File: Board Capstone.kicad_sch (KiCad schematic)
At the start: 12 parts, among them J101 Power, J102 Conn_JetsonNano, J103 Status_LED, J104 Warning_LED, SW101 SW_Pairing, U101 SN74LV1T125DBV, U102 SN74LV1T125DBV

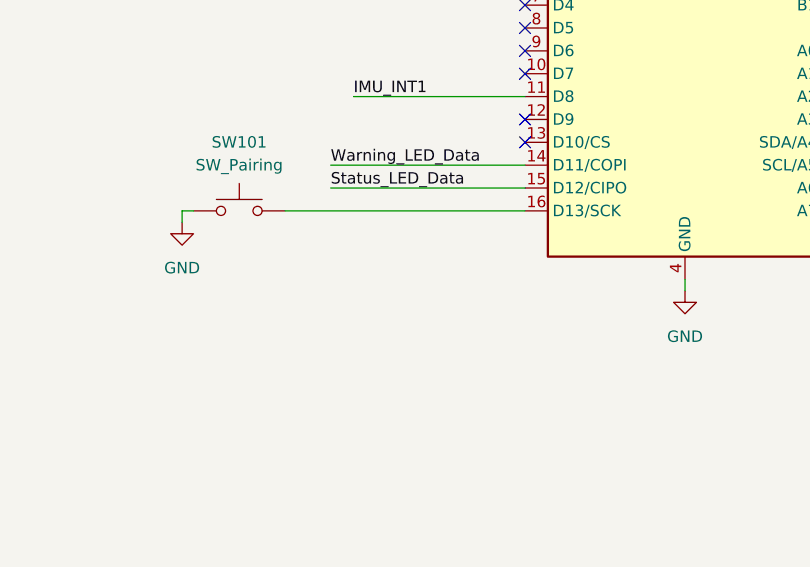
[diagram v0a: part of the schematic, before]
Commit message: rev 1.1.1 Added decoupling cap to push button
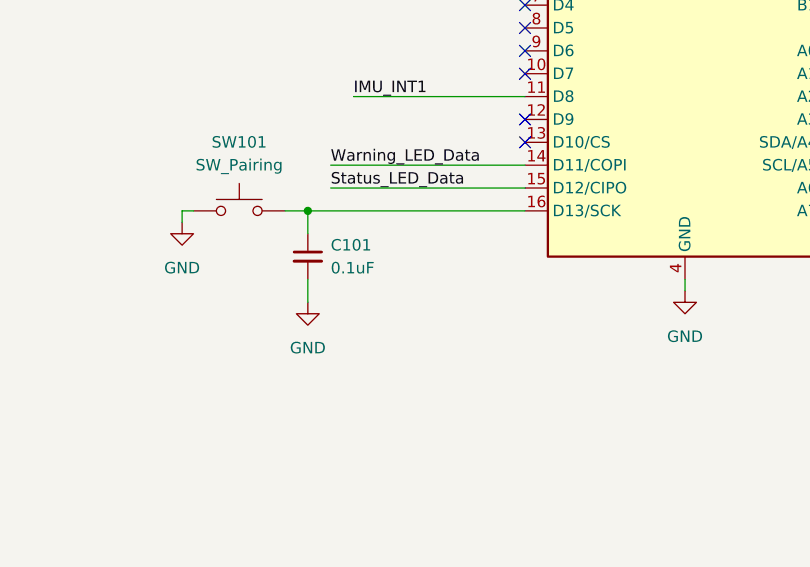
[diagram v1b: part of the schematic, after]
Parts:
- added C101: 0.1uF, Capacitor_SMD:C_1206_3216Metric_Pad1.33x1.80mm_HandSolder, symbol Device:C_Small
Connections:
- net GND: now also C101.2
- net at A101.16 (D13/SCK), SW101.2: now also C101.1
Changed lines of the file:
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@@
 		(title "Cyclops (Team 30)")
 		(date "2025-11-28")
-		(rev "1")
+		(rev "1.1.1")
 		(company "Concordia University, Department of Electrical and Computer Engineering")
 	)
@@
 	)
 	(junction
+		(at 111.76 83.82)
+		(diameter 0)
+		(color 0 0 0 0)
+	)
+	(junction
 		(at 208.28 76.2)
 		(diameter 0)
@@
 	(wire
 		(pts
+			(xy 111.76 83.82) (xy 135.89 83.82)
+		)
+		(stroke
+			(width 0)
+			(type default)
+		)
+	)
+	(wire
+		(pts
 			(xy 229.87 149.86) (xy 227.33 149.86)
 		)
@@
 	(wire
 		(pts
+			(xy 111.76 86.36) (xy 111.76 83.82)
+		)
+		(stroke
+			(width 0)
+			(type default)
+		)
+	)
+	(wire
+		(pts
 			(xy 24.13 41.91) (xy 24.13 43.18)
 		)
@@
 	(wire
 		(pts
-			(xy 109.22 83.82) (xy 135.89 83.82)
+			(xy 109.22 83.82) (xy 111.76 83.82)
 		)
 		(stroke
@@
 		(pts
 			(xy 24.13 45.72) (xy 24.13 46.99)
+		)
+		(stroke
+			(width 0)
+			(type default)
+		)
+	)
+	(wire
+		(pts
+			(xy 111.76 93.98) (xy 111.76 91.44)
 		)
 		(stroke
@@
 	(symbol
 		(lib_id "power:GND")
+		(at 111.76 93.98 0)
+		(unit 1)
+		(exclude_from_sim no)
+		(in_bom yes)
+		(on_board yes)
+		(dnp no)
+		(fields_autoplaced yes)
+		(property "Reference" "#PWR0122"
+			(at 111.76 100.33 0)
+			(effects
+				(font
+					(size 1.27 1.27)
+				)
+				(hide yes)
+			)
+		)
+		(property "Value" "GND"
+			(at 111.76 99.06 0)
+			(effects
+				(font
+					(size 1.27 1.27)
+				)
+			)
+		)
+		(property "Footprint" ""
+			(at 111.76 93.98 0)
+			(effects
+				(font
+					(size 1.27 1.27)
+				)
+				(hide yes)
+			)
+		)
+		(property "Datasheet" ""
+			(at 111.76 93.98 0)
+			(effects
+				(font
+					(size 1.27 1.27)
+				)
+				(hide yes)
+			)
+		)
+		(property "Description" "Power symbol creates a global label with name \"GND\" , ground"
+			(at 111.76 93.98 0)
+			(effects
+				(font
+					(size 1.27 1.27)
+				)
+				(hide yes)
+			)
+		)
+		(pin "1"
+		)
+		(instances
+			(project "Board Capstone"
+				(path "/9d0eb231-e921-459f-b79b-e47a090bee4f"
+					(reference "#PWR0122")
+					(unit 1)
+				)
+			)
+		)
+	)
+	(symbol
+		(lib_id "power:GND")
 		(at 203.2 124.46 0)
 		(unit 1)
@@
 					(unit 1)
 				)
+			)
+		)
+	)
+	(symbol
+		(lib_id "Device:C_Small")
+		(at 111.76 88.9 0)
+		(unit 1)
+		(exclude_from_sim no)
+		(in_bom yes)
+		(on_board yes)
+		(dnp no)
+		(fields_autoplaced yes)
+		(property "Reference" "C101"
+			(at 114.3 87.6362 0)
+			(effects
+				(font
+					(size 1.27 1.27)
+				)
+				(justify left)
+			)
+		)
+		(property "Value" "0.1uF"
+			(at 114.3 90.1762 0)
+			(effects
+				(font
+					(size 1.27 1.27)
+				)
+				(justify left)
+			)
+		)
+		(property "Footprint" "Capacitor_SMD:C_1206_3216Metric_Pad1.33x1.80mm_HandSolder"
+			(at 111.76 88.9 0)
+			(effects
+				(font
+					(size 1.27 1.27)
+				)
+				(hide yes)
+			)
+		)
+		(property "Datasheet" "~"
+			(at 111.76 88.9 0)
+			(effects
+				(font
+					(size 1.27 1.27)
+				)
+				(hide yes)
+			)
+		)
+		(property "Description" "Unpolarized capacitor, small symbol"
+			(at 111.76 88.9 0)
+			(effects
+				(font
+					(size 1.27 1.27)
+				)
+				(hide yes)
+			)
+		)
+		(pin "2"
+		)
+		(pin "1"
+		)
+		(instances
+			(project ""
+				(path "/9d0eb231-e921-459f-b79b-e47a090bee4f"
+					(reference "C101")
+					(unit 1)
+				)

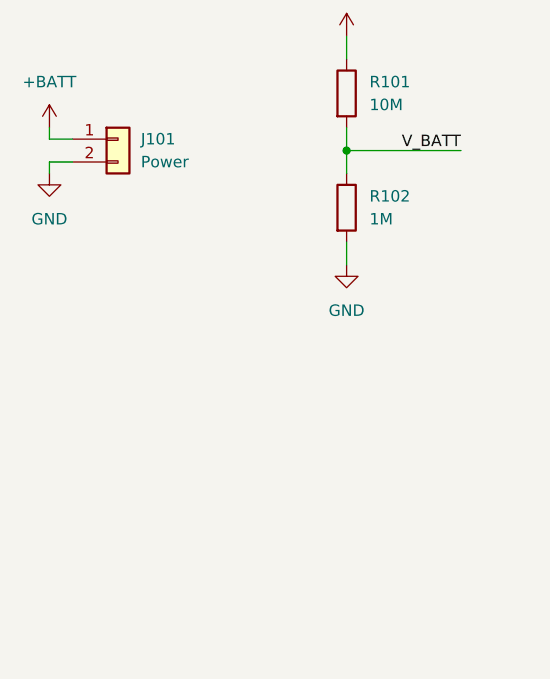
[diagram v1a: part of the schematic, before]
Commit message: Rev 1.2 Add 12v buck converter
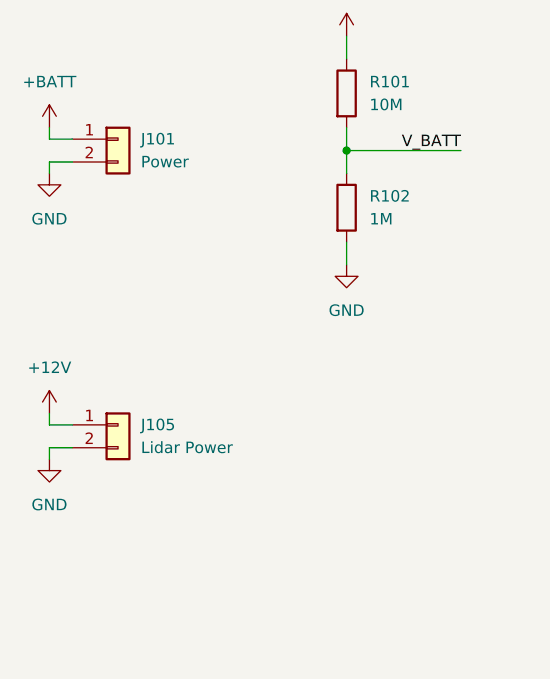
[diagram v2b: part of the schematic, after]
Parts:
- added J105: Lidar Power, Connector_JST:JST_XH_B2B-XH-A_1x02_P2.50mm_Vertical, symbol Connector_Generic:Conn_01x02
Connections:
- net GND: now also J105.2 (Pin_2)
- new net +12V: J105.1 (Pin_1)
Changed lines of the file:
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@@
 	(title_block
 		(title "Cyclops (Team 30)")
-		(date "2025-11-28")
-		(rev "1.1.1")
+		(date "2025-12-07")
+		(rev "1.2")
 		(company "Concordia University, Department of Electrical and Computer Engineering")
 	)
@@
 	(wire
 		(pts
+			(xy 26.67 77.47) (xy 24.13 77.47)
+		)
+		(stroke
+			(width 0)
+			(type default)
+		)
+	)
+	(wire
+		(pts
 			(xy 195.58 149.86) (xy 194.31 149.86)
 		)
@@
 	(wire
 		(pts
-			(xy 26.67 45.72) (xy 24.13 45.72)
+			(xy 26.67 74.93) (xy 24.13 74.93)
 		)
 		(stroke
@@
 	(wire
 		(pts
+			(xy 24.13 45.72) (xy 26.67 45.72)
+		)
+		(stroke
+			(width 0)
+			(type default)
+		)
+	)
+	(wire
+		(pts
 			(xy 24.13 41.91) (xy 24.13 43.18)
 		)
@@
 	(wire
 		(pts
+			(xy 24.13 73.66) (xy 24.13 74.93)
+		)
+		(stroke
+			(width 0)
+			(type default)
+		)
+	)
+	(wire
+		(pts
 			(xy 208.28 76.2) (xy 208.28 78.74)
 		)
@@
 		(pts
 			(xy 171.45 45.72) (xy 179.07 45.72)
+		)
+		(stroke
+			(width 0)
+			(type default)
+		)
+	)
+	(wire
+		(pts
+			(xy 24.13 77.47) (xy 24.13 78.74)
 		)
 		(stroke
@@
 	)
 	(symbol
+		(lib_id "power:GND")
+		(at 24.13 46.99 0)
+		(unit 1)
+		(exclude_from_sim no)
+		(in_bom yes)
+		(on_board yes)
+		(dnp no)
+		(fields_autoplaced yes)
+		(property "Reference" "#PWR0102"
+			(at 24.13 53.34 0)
+			(effects
+				(font
+					(size 1.27 1.27)
+				)
+				(hide yes)
+			)
+		)
+		(property "Value" "GND"
+			(at 24.13 52.07 0)
+			(effects
+				(font
+					(size 1.27 1.27)
+				)
+			)
+		)
+		(property "Footprint" ""
+			(at 24.13 46.99 0)
+			(effects
+				(font
+					(size 1.27 1.27)
+				)
+				(hide yes)
+			)
+		)
+		(property "Datasheet" ""
+			(at 24.13 46.99 0)
+			(effects
+				(font
+					(size 1.27 1.27)
+				)
+				(hide yes)
+			)
+		)
+		(property "Description" "Power symbol creates a global label with name \"GND\" , ground"
+			(at 24.13 46.99 0)
+			(effects
+				(font
+					(size 1.27 1.27)
+				)
+				(hide yes)
+			)
+		)
+		(pin "1"
+		)
+		(instances
+			(project "Board Capstone"
+				(path "/9d0eb231-e921-459f-b79b-e47a090bee4f"
+					(reference "#PWR0102")
+					(unit 1)
+				)
+			)
+		)
+	)
+	(symbol
 		(lib_id "power:+3.3V")
 		(at 208.28 74.93 0)
@@
 	(symbol
 		(lib_id "power:GND")
-		(at 24.13 46.99 0)
+		(at 24.13 78.74 0)
 		(unit 1)
 		(exclude_from_sim no)
@@
 		(dnp no)
 		(fields_autoplaced yes)
-		(property "Reference" "#PWR0102"
-			(at 24.13 53.34 0)
+		(property "Reference" "#PWR0124"
+			(at 24.13 85.09 0)
 			(effects
 				(font
@@
 		)
 		(property "Value" "GND"
-			(at 24.13 52.07 0)
+			(at 24.13 83.82 0)
 			(effects
 				(font
@@
 		)
 		(property "Footprint" ""
-			(at 24.13 46.99 0)
+			(at 24.13 78.74 0)
 			(effects
 				(font
@@
 		)
 		(property "Datasheet" ""
-			(at 24.13 46.99 0)
+			(at 24.13 78.74 0)
 			(effects
 				(font
@@
 		)
 		(property "Description" "Power symbol creates a global label with name \"GND\" , ground"
-			(at 24.13 46.99 0)
+			(at 24.13 78.74 0)
 			(effects
 				(font
@@
 		)
 		(instances
-			(project ""
+			(project "Board Capstone"
 				(path "/9d0eb231-e921-459f-b79b-e47a090bee4f"
-					(reference "#PWR0102")
-					(unit 1)
-				)
-			)
-		)
-	)
-	(symbol
-		(lib_id "Connector_Generic:Conn_01x02")
-		(at 31.75 43.18 0)
-		(unit 1)
-		(exclude_from_sim no)
-		(in_bom yes)
-		(on_board yes)
-		(dnp no)
-		(fields_autoplaced yes)
-		(property "Reference" "J101"
-			(at 34.29 43.1799 0)
-			(effects
-				(font
-					(size 1.27 1.27)
-				)
-				(justify left)
-			)
-		)
-		(property "Value" "Power"
-			(at 34.29 45.7199 0)
-			(effects
-				(font
-					(size 1.27 1.27)
-				)
-				(justify left)
-			)
-		)
-		(property "Footprint" "Connector_JST:JST_XH_B2B-XH-A_1x02_P2.50mm_Vertical"
-			(at 31.75 43.18 0)
-			(effects
-				(font
-					(size 1.27 1.27)
-				)
-				(hide yes)
-			)
-		)
-		(property "Datasheet" "~"
-			(at 31.75 43.18 0)
-			(effects
-				(font
-					(size 1.27 1.27)
-				)
-				(hide yes)
-			)
-		)
-		(property "Description" "Generic connector, single row, 01x02, script generated (kicad-library-utils/schlib/autogen/connector/)"
-			(at 31.75 43.18 0)
-			(effects
-				(font
-					(size 1.27 1.27)
-				)
-				(hide yes)
-			)
-		)
-		(pin "2"
-		)
-		(pin "1"
-		)
-		(instances
-			(project ""
-				(path "/9d0eb231-e921-459f-b79b-e47a090bee4f"
-					(reference "J101")
+					(reference "#PWR0124")
 					(unit 1)
 				)
@@
 	)
 	(symbol
+		(lib_id "power:+12V")
+		(at 24.13 73.66 0)
+		(unit 1)
+		(exclude_from_sim no)
+		(in_bom yes)
+		(on_board yes)
+		(dnp no)
+		(fields_autoplaced yes)
+		(property "Reference" "#PWR0123"
+			(at 24.13 77.47 0)
+			(effects
+				(font
+					(size 1.27 1.27)
+				)
+				(hide yes)
+			)
+		)
+		(property "Value" "+12V"
+			(at 24.13 68.58 0)
+			(effects
+				(font
+					(size 1.27 1.27)
+				)
+			)
+		)
+		(property "Footprint" ""
+			(at 24.13 73.66 0)
+			(effects
+				(font
+					(size 1.27 1.27)
+				)
+				(hide yes)
+			)
+		)
+		(property "Datasheet" ""
+			(at 24.13 73.66 0)
+			(effects
+				(font
+					(size 1.27 1.27)
+				)
+				(hide yes)
+			)
+		)
+		(property "Description" "Power symbol creates a global label with name \"+12V\""
+			(at 24.13 73.66 0)
+			(effects
+				(font
+					(size 1.27 1.27)
+				)
+				(hide yes)
+			)
+		)
+		(pin "1"
+		)
+		(instances
+			(project ""
+				(path "/9d0eb231-e921-459f-b79b-e47a090bee4f"
+					(reference "#PWR0123")
+					(unit 1)
+				)
+			)
+		)
+	)
+	(symbol
 		(lib_id "Device:R")
 		(at 57.15 38.1 0)
@@
 					(unit 1)
 				)
+			)
+		)
+	)
+	(symbol
+		(lib_name "Conn_01x02_2")
+		(lib_id "Connector_Generic:Conn_01x02")
+		(at 31.75 43.18 0)
+		(unit 1)
+		(exclude_from_sim no)
+		(in_bom yes)
+		(on_board yes)
+		(dnp no)
+		(fields_autoplaced yes)
+		(property "Reference" "J101"
+			(at 34.29 43.1799 0)
+			(effects
+				(font
+					(size 1.27 1.27)
+				)
+				(justify left)
+			)
+		)
+		(property "Value" "Power"
+			(at 34.29 45.7199 0)
+			(effects
+				(font
+					(size 1.27 1.27)
+				)
+				(justify left)
+			)
+		)
+		(property "Footprint" "Connector_JST:JST_XH_B2B-XH-A_1x02_P2.50mm_Vertical"
+			(at 31.75 43.18 0)
+			(effects
+				(font
+					(size 1.27 1.27)
+				)
+				(hide yes)
+			)
+		)
+		(property "Datasheet" "~"
+			(at 31.75 43.18 0)
+			(effects
+				(font
+					(size 1.27 1.27)
+				)
+				(hide yes)
+			)
+		)
+		(property "Description" "Generic connector, single row, 01x02, script generated (kicad-library-utils/schlib/autogen/connector/)"
+			(at 31.75 43.18 0)
+			(effects
+				(font
+					(size 1.27 1.27)
+				)
+				(hide yes)
+			)
+		)
+		(pin "1"
+		)
+		(pin "2"
+		)
+		(instances
+			(project "Board Capstone"
+				(path "/9d0eb231-e921-459f-b79b-e47a090bee4f"
+					(reference "J101")
+					(unit 1)
+				)
+			)
+		)
+	)
+	(symbol
+		(lib_name "Conn_01x02_1")
+		(lib_id "Connector_Generic:Conn_01x02")
+		(at 31.75 74.93 0)
+		(unit 1)
+		(exclude_from_sim no)
+		(in_bom yes)
+		(on_board yes)
+		(dnp no)
+		(fields_autoplaced yes)
+		(property "Reference" "J105"
+			(at 34.29 74.9299 0)
+			(effects
+				(font
+					(size 1.27 1.27)
+				)
+				(justify left)
+			)
+		)
+		(property "Value" "Lidar Power"
+			(at 34.29 77.4699 0)
+			(effects
+				(font
+					(size 1.27 1.27)
+				)
+				(justify left)
+			)
+		)
+		(property "Footprint" "Connector_JST:JST_XH_B2B-XH-A_1x02_P2.50mm_Vertical"
+			(at 31.75 74.93 0)
+			(effects
+				(font
+					(size 1.27 1.27)
+				)
+				(hide yes)
+			)
+		)
+		(property "Datasheet" "~"
+			(at 31.75 74.93 0)
+			(effects
+				(font
+					(size 1.27 1.27)
+				)
+				(hide yes)
+			)
+		)
+		(property "Description" "Generic connector, single row, 01x02, script generated (kicad-library-utils/schlib/autogen/connector/)"
+			(at 31.75 74.93 0)
+			(effects
+				(font
+					(size 1.27 1.27)
+				)
+				(hide yes)
+			)
+		)
+		(pin "1"
+		)
+		(pin "2"
+		)
+		(instances
+			(project ""
+				(path "/9d0eb231-e921-459f-b79b-e47a090bee4f"
+					(reference "J105")
+					(unit 1)
+				)
